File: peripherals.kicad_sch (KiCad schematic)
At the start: 35 parts, among them J8 Conn_01x06_Male, J9 Conn_01x04_MountingPin, U1 MIMX8MM6DVTLZAA, U31 TXB0104RUT, U32 TCA9803

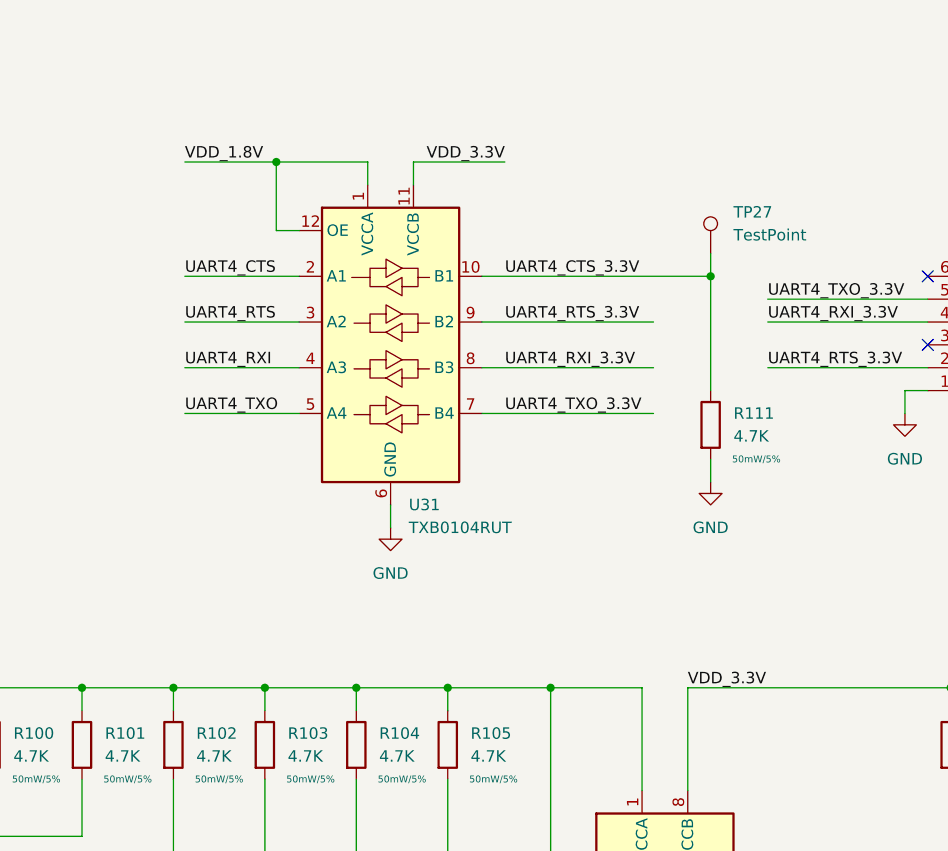
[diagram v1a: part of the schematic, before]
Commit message: bom work, change uart level shifter and m.2 socket
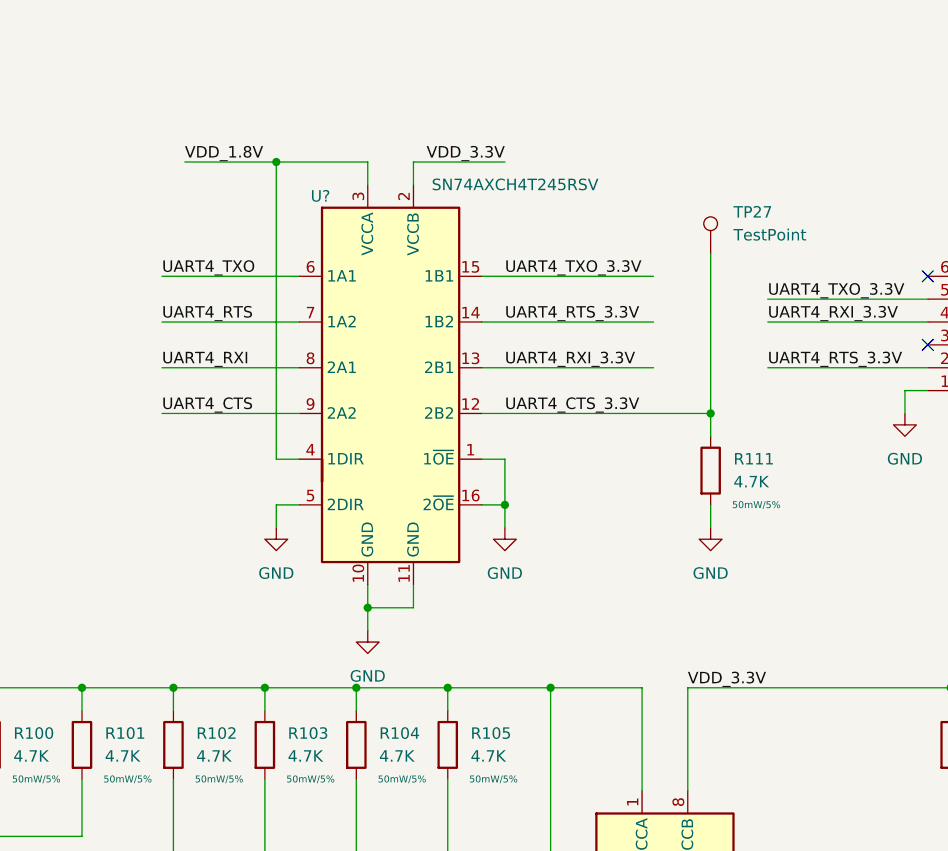
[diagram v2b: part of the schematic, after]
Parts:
- removed U31: TXB0104RUT, Package_DFN_QFN:Texas_R_PUQFN-N12, symbol Logic_LevelTranslator:TXB0104RUT
- added U?: SN74AXCH4T245RSV, qsbc:UQFN-16_1.6x2.4_Pitch0.4mm, symbol qsbc:SN74AXCH4T245RSV
- C144, C145, C146, C147: MPN (none) -> CL05A104KA5NNNC
- J8: MPN (none) -> M20-8890645
- J9: MPN (none) -> PRT-16766
- R100, R101, R102, R103, R104, R105, R111, R118, R121: MPN (none) -> RC0402JR-074K7L
- R106, R107, R109, R110, R112, R113, R115, R116, R117, R119, R120, R122, R123, R124, R125, R126: DigiKey_PN 311-10KJRCT-ND -> (none); MPN RC0402JR-0710KL -> RC0402FR-0710KL
- U1: MPN (none) -> MIMX8MM6DVTLZAA
- U32: MPN (none) -> TCA9803DGKR
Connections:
- net GND: now also U?.1 (1~{OE}), U?.10 (GND), U?.11 (GND), U?.16 (2~{OE}), U?.5 (2DIR)
- net UART4_CTS: now also U?.9 (2A2)
- net UART4_CTS_3.3V: now also U?.12 (2B2)
- net UART4_RTS: now also U?.7 (1A2)
- net UART4_RTS_3.3V: now also U?.14 (1B2)
- net UART4_RXI: now also U?.8 (2A1)
- net UART4_RXI_3.3V: now also U?.13 (2B1)
- net UART4_TXO: now also U?.6 (1A1)
- net UART4_TXO_3.3V: now also U?.15 (1B1)
- net VDD_1.8V: now also U?.3 (VCCA), U?.4 (1DIR)
- net VDD_3.3V: now also U?.2 (VCCB)
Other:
- moved on the sheet: R111

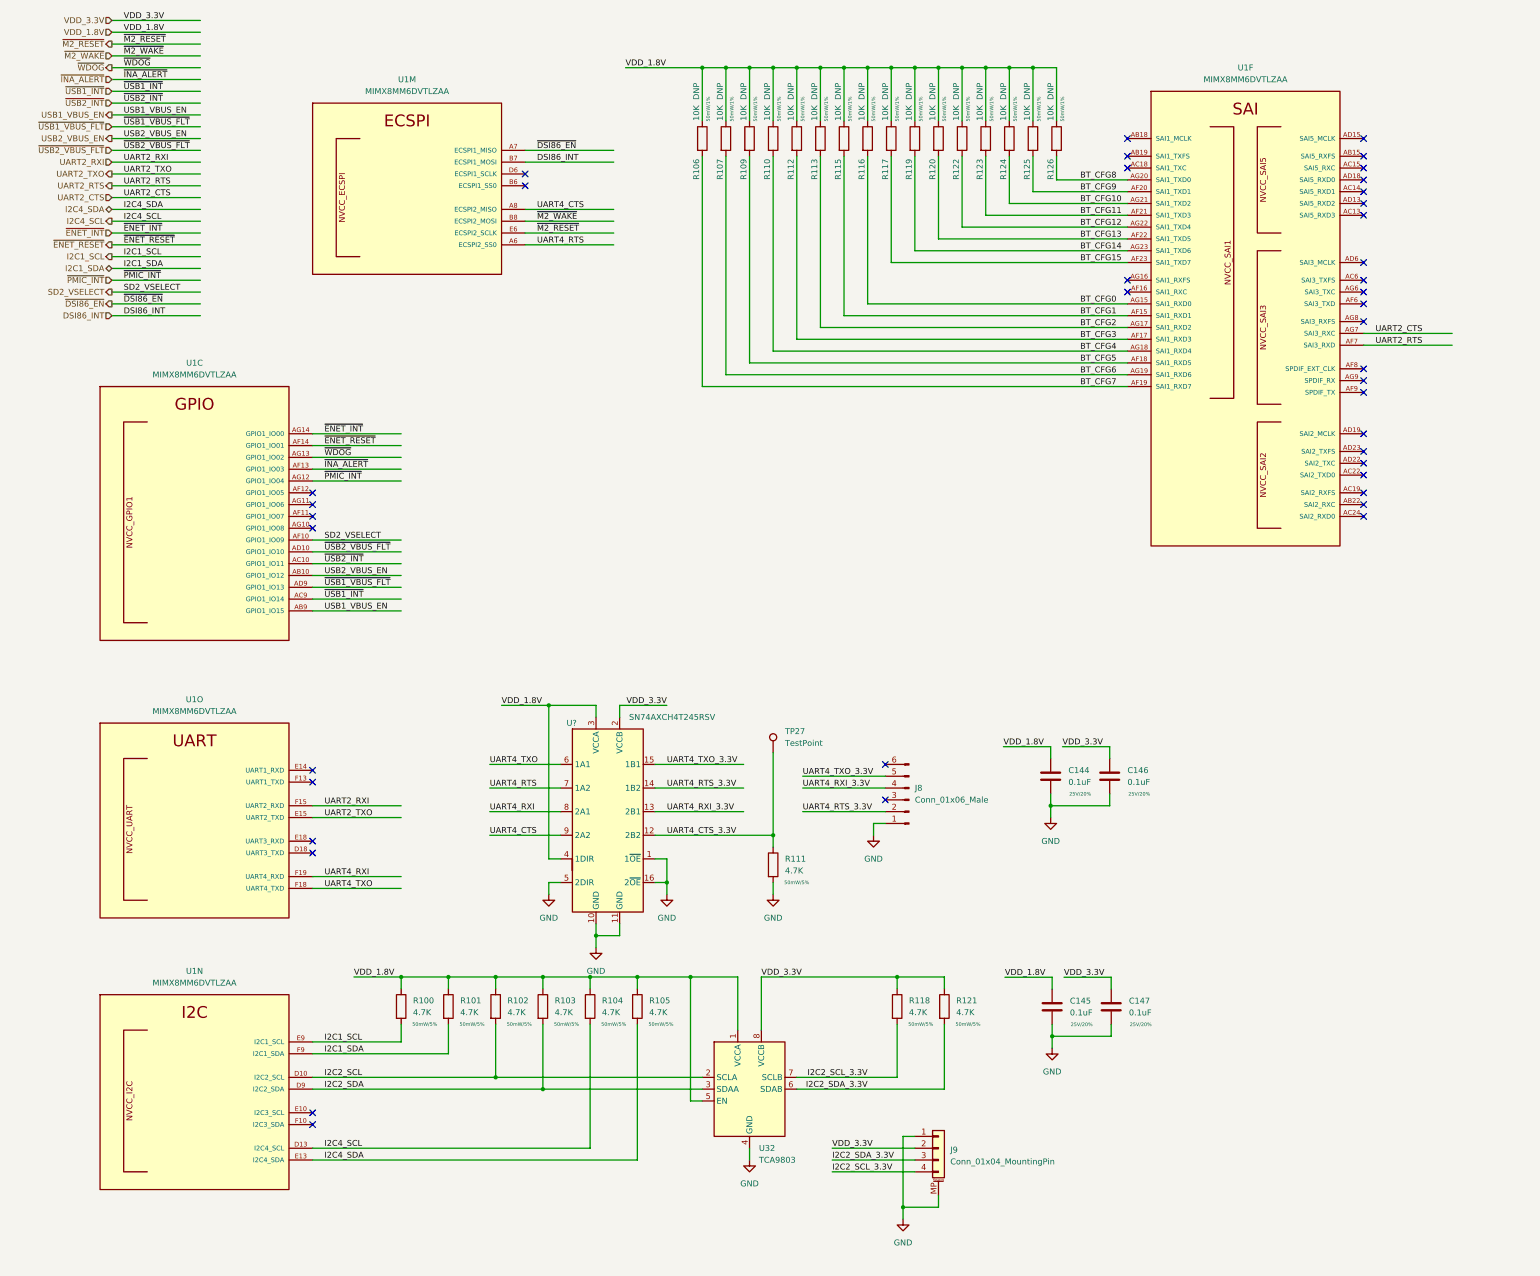
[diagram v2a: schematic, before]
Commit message: ddr length matching work, misc cleanup
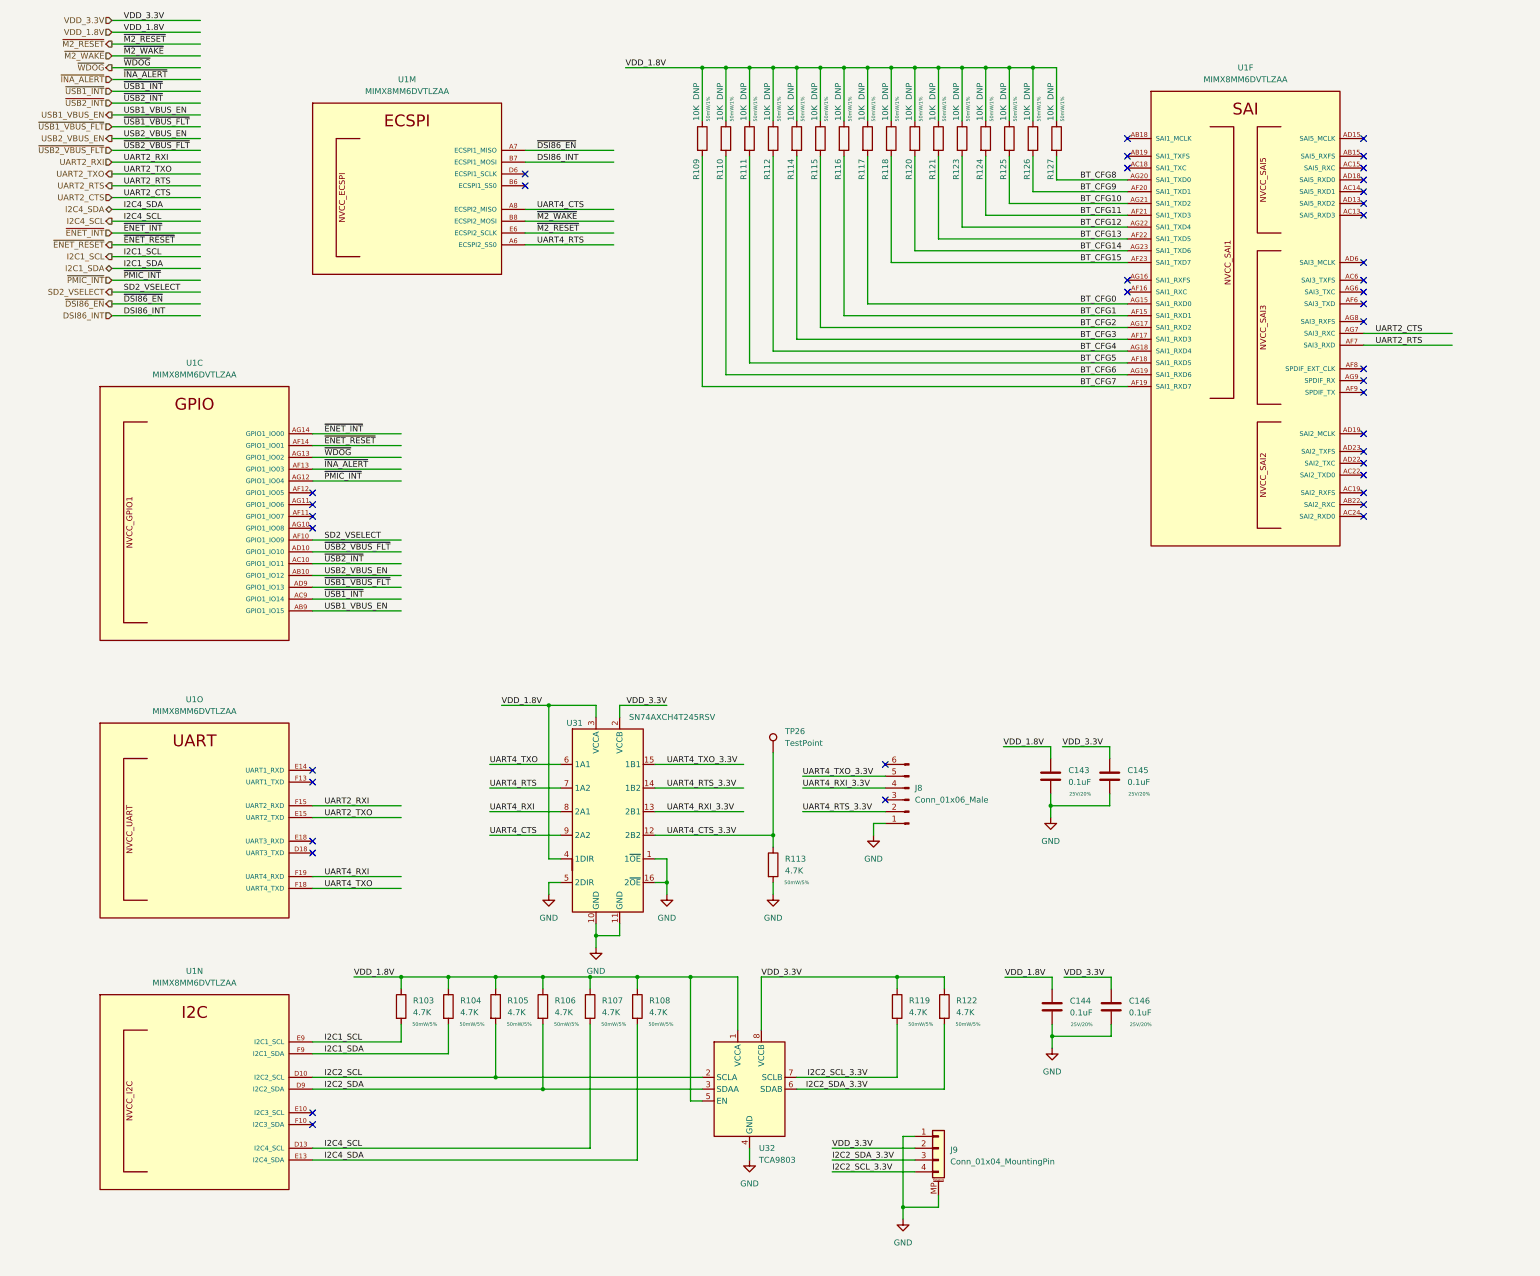
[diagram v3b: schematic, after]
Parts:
- gave numbers to parts that had none: 1
- renumbered C144 to C143, C145 to C144, C146 to C145, C147 to C146, R100 to R103, R101 to R104, R102 to R105, R103 to R106, R104 to R107, R105 to R108, R106 to R109, R107 to R110, R109 to R111, R110 to R112, R111 to R113, R112 to R114, R113 to R115, R115 to R116, R116 to R117, R117 to R118, R118 to R119, R119 to R120, R120 to R121, R121 to R122, R122 to R123, R123 to R124, R124 to R125, R125 to R126, R126 to R127, TP27 to TP26

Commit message: misc cleanup, change from usb mux to dual uart
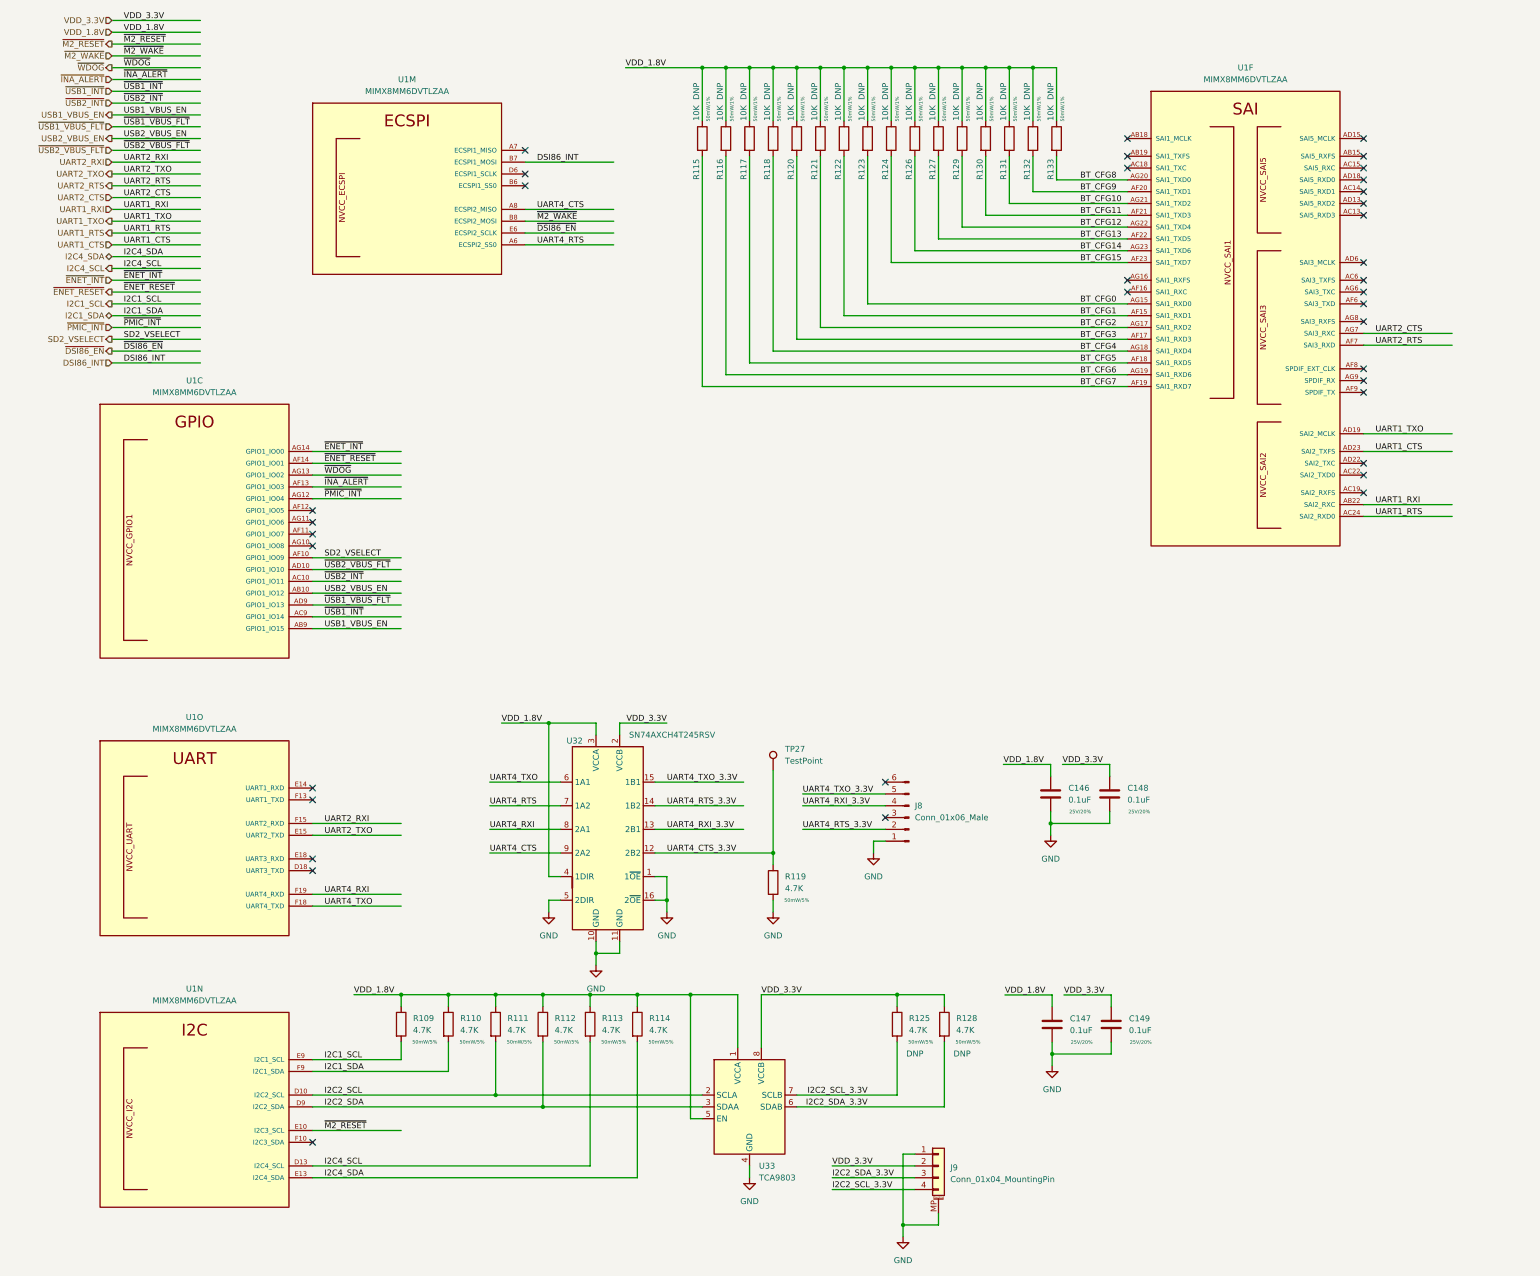
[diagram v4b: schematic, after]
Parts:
- R125: renamed from R119; DNP (none) -> DNP
- R128: renamed from R122; DNP (none) -> DNP
- TP27: renamed from TP26; now left out of the parts list
- renumbered C143 to C146, C144 to C147, C145 to C148, C146 to C149, R103 to R109, R104 to R110, R105 to R111, R106 to R112, R107 to R113, R108 to R114, R109 to R115, R110 to R116, R111 to R117, R112 to R118, R113 to R119, R114 to R120, R115 to R121, R116 to R122, R117 to R123, R118 to R124, R120 to R126, R121 to R127, R123 to R129, R124 to R130, R125 to R131, R126 to R132, R127 to R133, U31 to U32, U32 to U33
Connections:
- net ~{DSI86_EN}: now also U1.E6 (ECSPI2_SCLK); no longer U1.A7 (ECSPI1_MISO)
- net ~{M2_RESET}: now also U1.E10 (I2C3_SCL); no longer U1.E6 (ECSPI2_SCLK)
- net UART1_RXI: now reaches U1.AB22 (SAI2_RXC)
- net UART1_RTS: now reaches U1.AC24 (SAI2_RXD0)
- net UART1_TXO: now reaches U1.AD19 (SAI2_MCLK)
- net UART1_CTS: now reaches U1.AD23 (SAI2_TXFS)
- no-connect marks 41 -> 37
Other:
- moved on the sheet: C146, C147, C148, C149, J8, J9, R109, R110, R111, R112, R113, R114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

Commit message: Rev 1
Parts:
- renumbered R109 to R108, R110 to R109, R111 to R110, R112 to R111, R113 to R112, R114 to R113, R115 to R114, R116 to R115, R117 to R116, R118 to R117, R119 to R118, R120 to R119, R121 to R120, R122 to R121, R123 to R122, R124 to R123, R125 to R124, R126 to R125, R127 to R126, R128 to R127, R129 to R128, R130 to R129, R131 to R130, R132 to R131, R133 to R132, TP27 to TP28
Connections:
- net VDD_1.8V: now also U1.AC14 (SAI5_RXD1)
- no-connect marks 37 -> 36
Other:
- note added: "Board Revision Straps SAI5_RXD[3:1] 001 - Rev 1.0"

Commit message: misc changes for rev1
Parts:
- R114, R115, R116, R117, R119, R120, R121, R122, R123, R124, R126, R127, R128, R129, R130, R131, R132: now left out of the parts list
- U32: value SN74AXCH4T245RSV -> 74AXCH4T245; MPN (none) -> SN74AXCH4T245RSVR
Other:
- note added: "TODO: UART1_TXO Should be on SAI2_RXFS"
- note added: "TODO: USB*_VBUS_FLT should be on USB PHY OC pad"
- moved on the sheet: C146, C148, J8, R118, TP28, U32

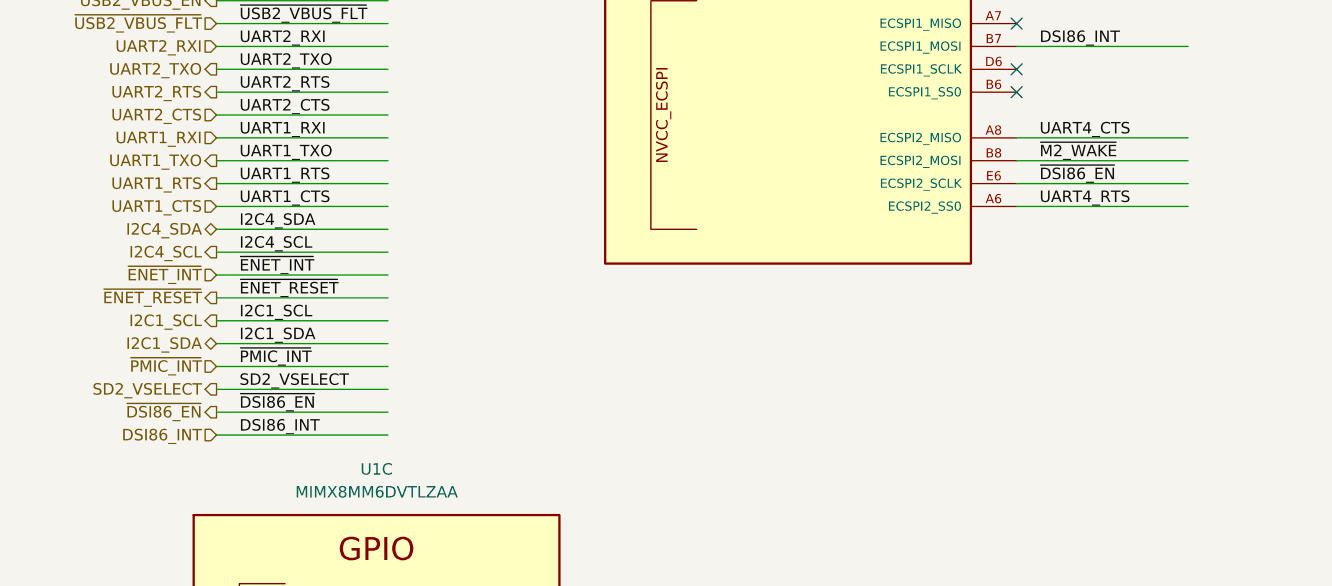
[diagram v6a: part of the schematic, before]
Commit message: dsi86: en is active high
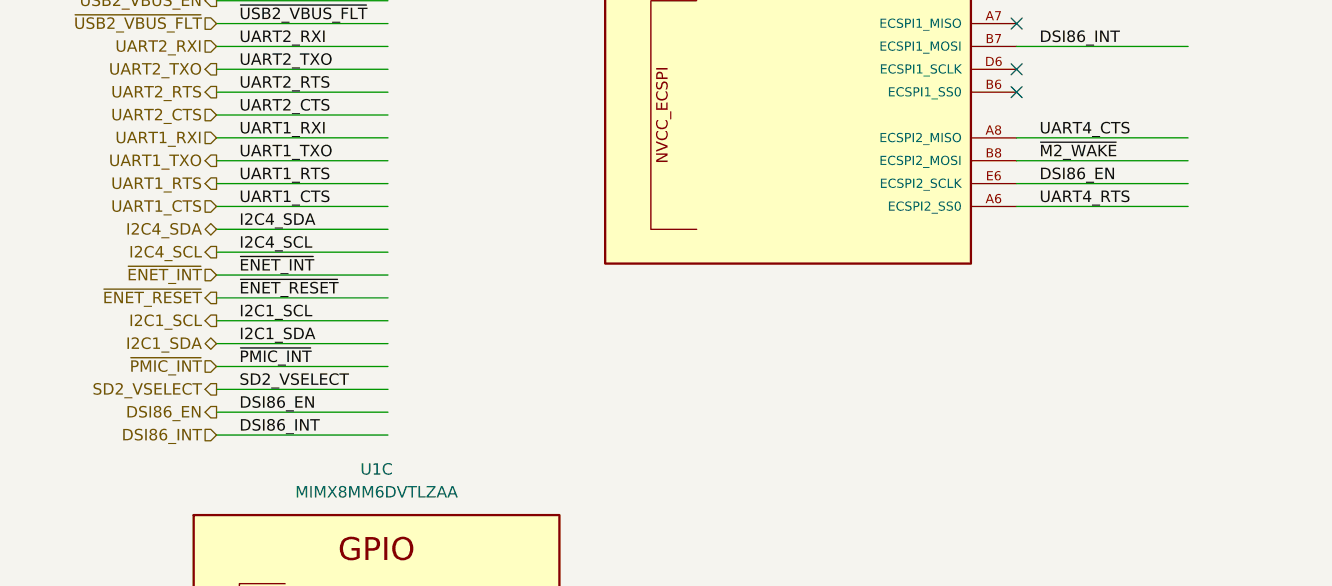
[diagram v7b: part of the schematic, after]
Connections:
- net ~{DSI86_EN} renamed DSI86_EN
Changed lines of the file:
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@@
     (effects (font (size 1.27 1.27)) (justify left bottom))
   )
-  (label "~{DSI86_EN}" (at 36.83 86.36 0)
+  (label "DSI86_EN" (at 36.83 86.36 0)
     (effects (font (size 1.27 1.27)) (justify left bottom))
   )
@@
     (effects (font (size 1.27 1.27)) (justify left bottom))
   )
-  (label "~{DSI86_EN}" (at 125.73 60.96 0)
+  (label "DSI86_EN" (at 125.73 60.96 0)
     (effects (font (size 1.27 1.27)) (justify left bottom))
   )
@@
     (effects (font (size 1.27 1.27)) (justify right))
   )
-  (hierarchical_label "~{DSI86_EN}" (shape output) (at 34.29 86.36 180)
-    (effects (font (size 1.27 1.27)) (justify right))
-  )
+  (hierarchical_label "DSI86_EN" (shape output) (at 34.29 86.36 180)
+    (effects (font (size 1.27 1.27)) (justify right))
+  )

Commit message: fixup qwiic con p/n, fixup dnp and values based on testing
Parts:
- J9: MPN PRT-16766 -> PRT-14417
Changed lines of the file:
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@@
       (effects (font (size 1.27 1.27)) hide)
     )
-    (property "MPN" "PRT-16766" (id 4) (at 212.09 261.62 0)
+    (property "MPN" "PRT-14417" (id 4) (at 212.09 261.62 0)
       (effects (font (size 1.27 1.27)) hide)
     )
